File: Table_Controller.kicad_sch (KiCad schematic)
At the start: 145 parts, among them J1 Dell DC jack, J11 HX JN1.27-2x5 WZ H4.9, J12 JST B4B XH A, J13 Conn_01x14_Pin, J14 JST B6B XH A, J15 2.54 mm header, J2 USB_C_Receptacle_USB2.0_16P, J3 DC barrel assy, U1 USBLC6-2SC6, U10 STM32G431K8Tx, U11 LMR380x0, U12 VNH7070, Y10 20 MHz

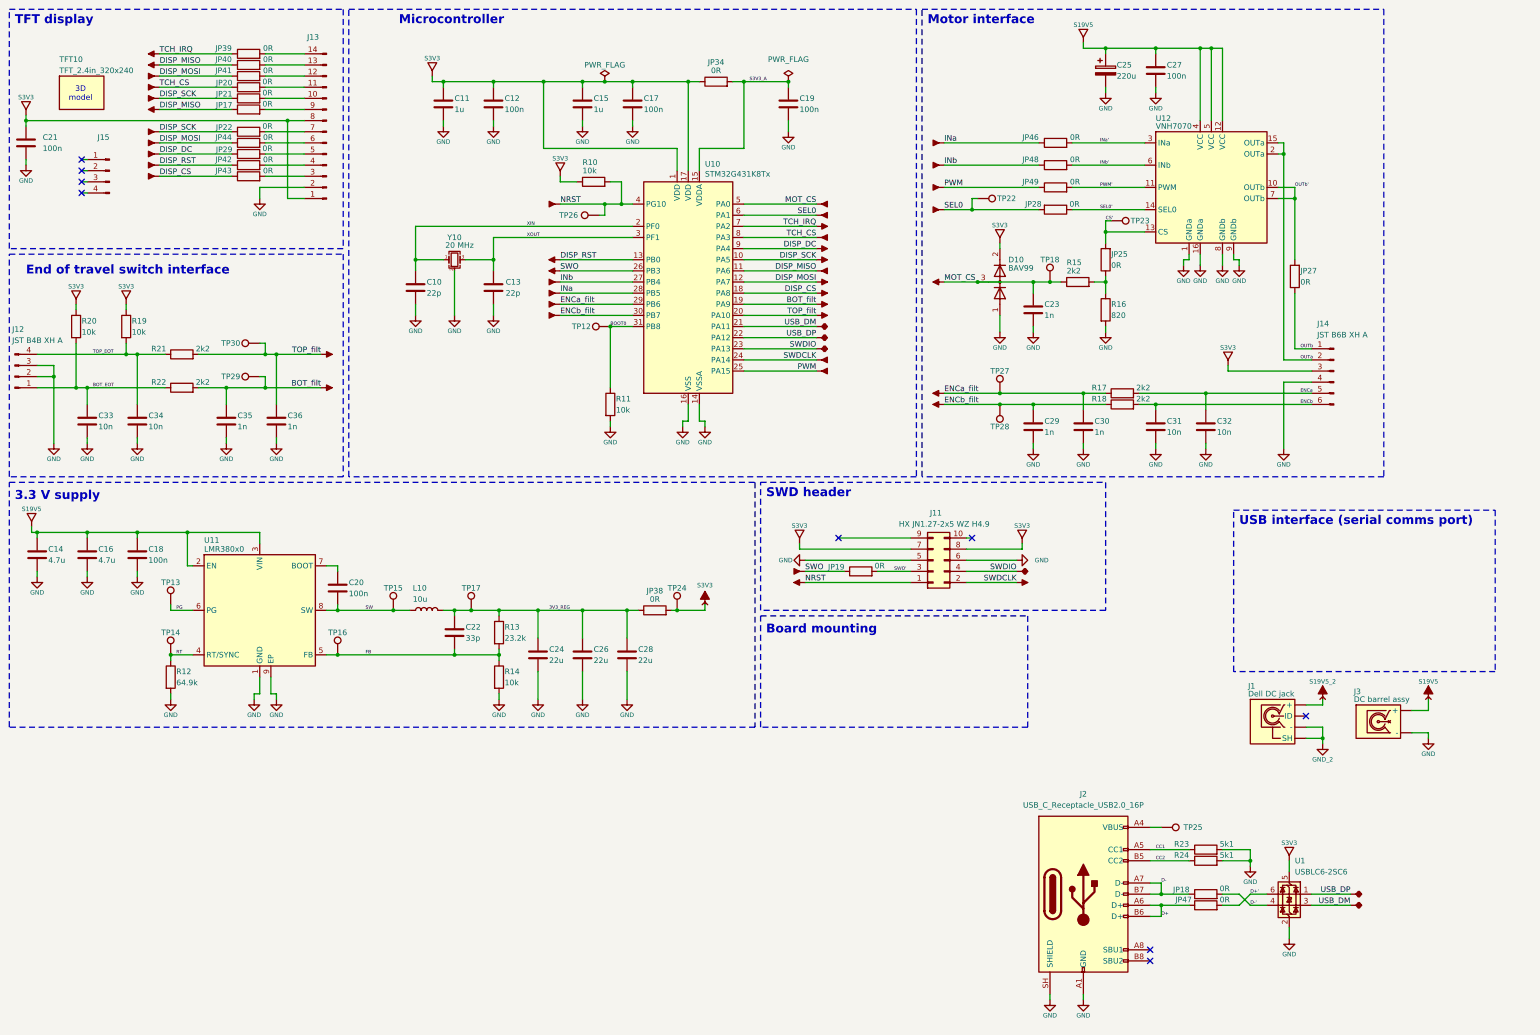
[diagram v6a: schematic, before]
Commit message: top silk done
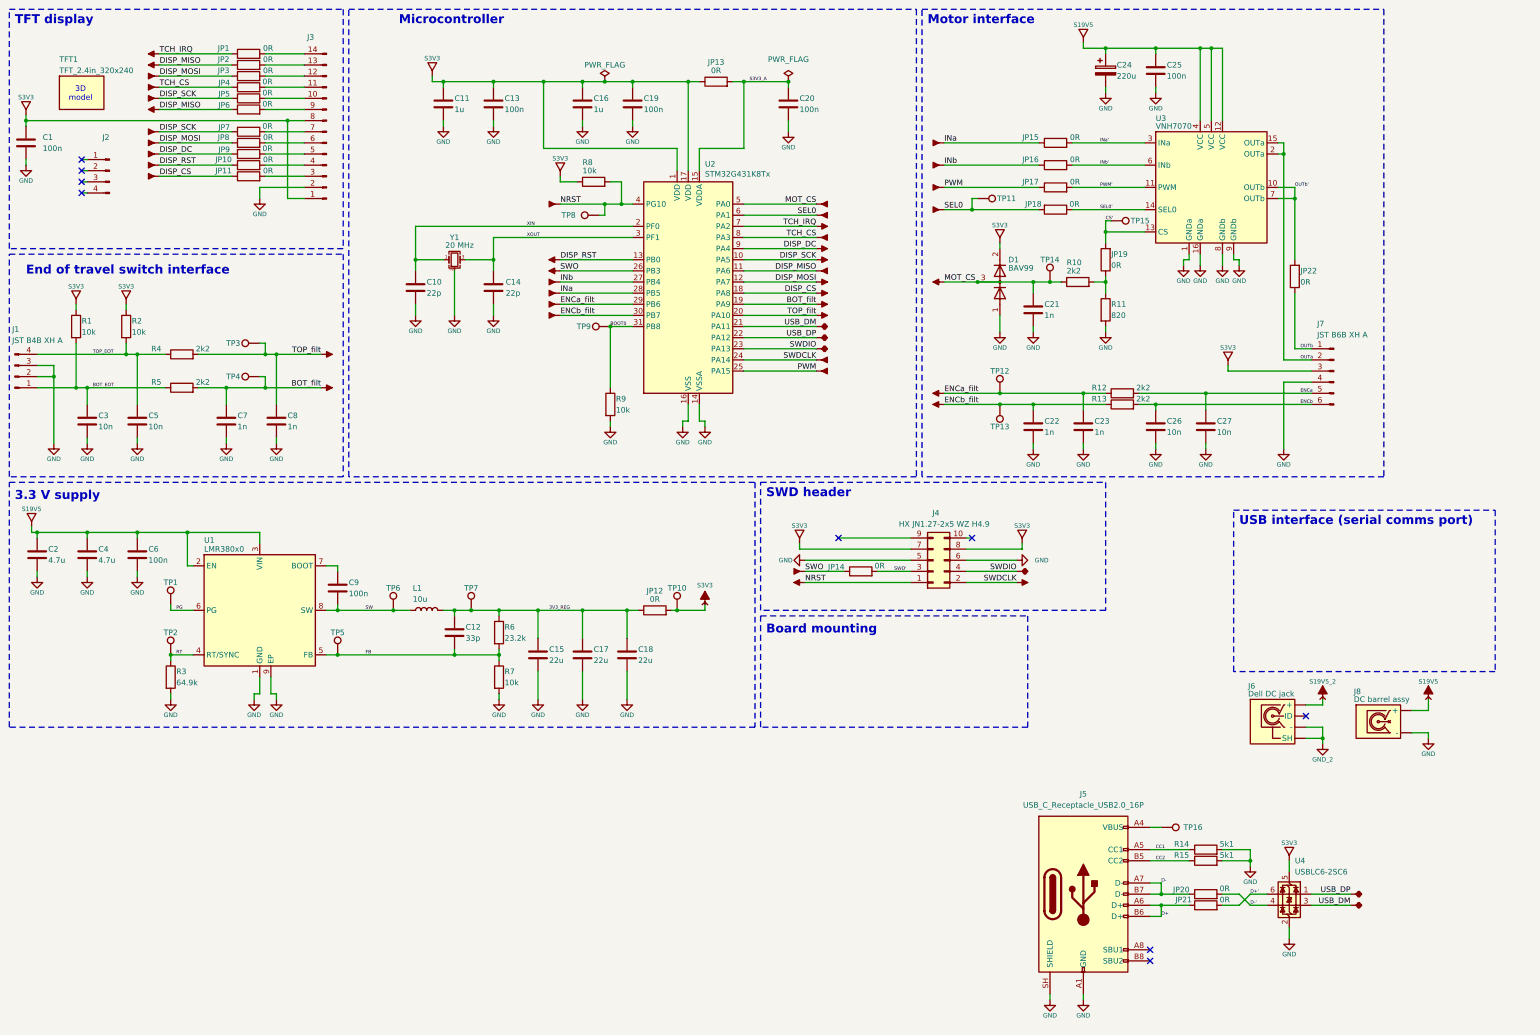
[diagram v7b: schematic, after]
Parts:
- renumbered C21 to C1, C22 to C12, C12 to C13, C13 to C14, C24 to C15, C15 to C16, C26 to C17, C28 to C18, C17 to C19, C14 to C2, C19 to C20, C23 to C21, C29 to C22, C30 to C23, C25 to C24, C27 to C25, C31 to C26, C32 to C27, C33 to C3, C16 to C4, C34 to C5, C18 to C6, C35 to C7, C36 to C8, C20 to C9, D10 to D1, J12 to J1, J15 to J2, J13 to J3, J11 to J4, J2 to J5, J1 to J6, J14 to J7, J3 to J8, JP39 to JP1, JP42 to JP10, JP43 to JP11, JP38 to JP12, JP34 to JP13, JP19 to JP14, JP46 to JP15, JP48 to JP16, JP49 to JP17, JP28 to JP18, JP25 to JP19, JP40 to JP2, JP18 to JP20, JP47 to JP21, JP27 to JP22, JP41 to JP3, JP20 to JP4, JP21 to JP5, JP17 to JP6, JP22 to JP7, JP44 to JP8, JP29 to JP9, L10 to L1, P40 to P1, P49 to P10, P50 to P11, P61 to P12, P62 to P13, P22 to P14, P16 to P15, P17 to P16, P18 to P17, P19 to P18, P20 to P19, P41 to P2, P21 to P20, P10 to P21, P11 to P22, P42 to P3, P51 to P39, P43 to P4, P52 to P40, P53 to P41, P54 to P42, P39 to P43, P57 to P44, P58 to P45, P12 to P46, P13 to P47, P81 to P48, P82 to P49, P44 to P5, P45 to P6, P46 to P7, P47 to P8, P48 to P9, R20 to R1, R15 to R10, R16 to R11, R17 to R12, R18 to R13, R23 to R14, R24 to R15, R19 to R2, R12 to R3, R21 to R4, R22 to R5, R13 to R6, R14 to R7, R10 to R8, R11 to R9, TFT10 to TFT1, TP13 to TP1, TP24 to TP10, TP22 to TP11, TP27 to TP12, TP28 to TP13, TP18 to TP14, TP23 to TP15, TP25 to TP16, TP14 to TP2, TP30 to TP3, TP29 to TP4, TP16 to TP5, TP15 to TP6, TP17 to TP7, TP26 to TP8, TP12 to TP9, U11 to U1, U10 to U2, U12 to U3, U1 to U4, Y10 to Y1

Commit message: layout ready for mfg review
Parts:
- added TP17, TP18, TP19, TP20, TP21: TestPoint, TestPoint:TestPoint_THTPad_D1.0mm_Drill0.5mm, symbol Connector:TestPoint
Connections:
- net GND: now also J8.2 (-), TP17.1, TP18.1, TP19.1, TP20.1, TP21.1; no longer J8.3 (-)
